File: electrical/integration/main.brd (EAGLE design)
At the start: 127 x 92 mm, 151 parts

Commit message: group components logically
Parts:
- moved POWER_TOP1:C2 558.5 mm to (-5.84, -14.9), flipped to the bottom, turned to 180 degrees
- moved POWER_TOP1:C3 529.0 mm to (5.52, -6.16), flipped to the bottom
- moved POWER_TOP1:R2 510.2 mm to (-9.82, -30.8), turned to 180 degrees
- moved POWER_TOP1:F2 493.8 mm to (-14.1, -14.9), flipped to the bottom
- moved POWER_TOP1:C4 480.6 mm to (36.3, -8.60), flipped to the bottom, turned to 270 degrees
- moved POWER_TOP1:R4 475.6 mm to (-12.4, 0.76), turned to 180 degrees
- moved POWER_TOP1:F1 469.6 mm to (28.1, -8.01), flipped to the bottom
- moved POWER_TOP1:MOV1 462.0 mm to (-5.66, -16.5), flipped to the bottom, turned to 180 degrees
- moved POWER_TOP1:LED1 455.6 mm to (-7.10, 0.70)
- moved POWER_TOP1:U$1 451.8 mm to (18.5, -3.90)
- moved POWER_TOP1:R3 445.0 mm to (36.4, -8.46), turned to 90 degrees
- moved POWER_TOP1:U$2 438.4 mm to (-9.63, -23.2), turned to 90 degrees
- moved POWER_TOP1:LED2 420.7 mm to (-4.43, -30.8)
- moved POWER_TOP1:MOV2 407.7 mm to (38.1, -8.58), flipped to the bottom, turned to 270 degrees
- moved MICROCONTROLLER1:R9 384.1 mm to (96.5, -67.3), turned to 90 degrees
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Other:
- board size 127 x 92 mm -> 168 x 104 mm

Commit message: replace mow enable toggle with connector. position connectors more
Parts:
- removed JETSON1:JETSON_TX2_J21_EXPANSION1:U$4, MICROCONTROLLER1:U$2, MICROCONTROLLER1:U$3: TSM-120-XX-XXX-DV, TSM-120-XX-XXX-DV:TSM-120-XX-XXX-D
- removed JETSON1:JETSON_TX2_J26_GPIO1:U$1, JETSON1:JETSON_TX2_J26_GPIO1:U$2: TSM-115-XX-XXX-DV, TSM-115-XX-XXX-DV:TSM-115-XX-XXX-D
- removed MOTOR_TOP1:MOTOR_ISO1:C3, MOTOR_TOP1:MOTOR_ISO2:C3: 1uF, rcl:C0603
- removed MOTOR_TOP1:MOTOR_ISO1:PAD1, MOTOR_TOP1:MOTOR_ISO2:PAD1: (no value), wirepad:1,6/0,8
- removed MOTOR_TOP1:MOTOR_ISO1:R1, MOTOR_TOP1:MOTOR_ISO1:R2, MOTOR_TOP1:MOTOR_ISO1:R5, MOTOR_TOP1:MOTOR_ISO2:R1, MOTOR_TOP1:MOTOR_ISO2:R2, MOTOR_TOP1:MOTOR_ISO2:R5: 47k, SparkFun-Resistors:0603
- removed MOTOR_TOP1:MOTOR_ISO1:R10, MOTOR_TOP1:MOTOR_ISO2:R10: 150k, SparkFun-Resistors:0603
- removed MOTOR_TOP1:MOTOR_ISO1:R3, MOTOR_TOP1:MOTOR_ISO1:R4, MOTOR_TOP1:MOTOR_ISO1:R6, MOTOR_TOP1:MOTOR_ISO1:R8, MOTOR_TOP1:MOTOR_ISO2:R3, MOTOR_TOP1:MOTOR_ISO2:R4, MOTOR_TOP1:MOTOR_ISO2:R6, MOTOR_TOP1:MOTOR_ISO2:R8: 1.20k, SparkFun-Resistors:0603
- removed MOTOR_TOP1:MOTOR_ISO1:R7, MOTOR_TOP1:MOTOR_ISO2:R7: 300k, SparkFun-Resistors:0603
- removed MOTOR_TOP1:MOTOR_ISO1:R9, MOTOR_TOP1:MOTOR_ISO2:R9: 330k, SparkFun-Resistors:0603
- removed MOTOR_TOP1:MOTOR_ISO1:U1, MOTOR_TOP1:MOTOR_ISO1:U2, MOTOR_TOP1:MOTOR_ISO1:U3, MOTOR_TOP1:MOTOR_ISO2:U1, MOTOR_TOP1:MOTOR_ISO2:U2, MOTOR_TOP1:MOTOR_ISO2:U3: SFH615A-3X009T, SFH615A-3X009T:SOIC254P1016X390-4N
- removed MOTOR_TOP1:MOTOR_ISO1:U4, MOTOR_TOP1:MOTOR_ISO2:U4: AMC1200SDUB, power_supplies:DUB8
- removed MOTOR_TOP1:MOTOR_ISO1:X1, MOTOR_TOP1:MOTOR_ISO2:X1: 43045-0609, con-molex-micro-fit-3_0:43045-0609
- removed RELAY_CONTROL_TOP1:RELAY_CONTROL1:S2: ST141D00, ST141D00:SW_ST141D00
- removed RELAY_CONTROL_TOP1:RELAY_CONTROL1:X1, RELAY_CONTROL_TOP1:RELAY_CONTROL1:X3, RELAY_CONTROL_TOP1:X3, RELAY_CONTROL_TOP1:X4: 43045-0209, con-molex-micro-fit-3_0:43045-0209
- added MOTOR_TOP1:JDL, MOTOR_TOP1:JDR: 43045-0609, con-molex-micro-fit-3_0:43045-0609
- added RELAY_CONTROL_TOP1:JBAT, RELAY_CONTROL_TOP1:JISO, RELAY_CONTROL_TOP1:RELAY_CONTROL1:JESTP, RELAY_CONTROL_TOP1:RELAY_CONTROL1:JMOW, RELAY_CONTROL_TOP1:RELAY_CONTROL1:JTHR: 43045-0209, con-molex-micro-fit-3_0:43045-0209
- moved SENSOR_TOP1:U1 97.9 mm to (91.6, -32.9)
- moved SENSOR_TOP1:ENCODER2:X1 97.6 mm to (24.0, -87.8)
- moved SENSOR_TOP1:ENCODER1:X1 97.5 mm to (40.9, -87.8)
- moved SENSOR_TOP1:REACH_GPS1:U$1 87.6 mm to (123.3, -77.9), turned to 90 degrees
- moved JETSON1:X1 84.7 mm to (-8.85, -45.5), turned to 0 degrees
- moved POWER_TOP1:R2 80.2 mm to (4.88, 48.0)
- moved POWER_TOP1:LED2 79.8 mm to (12.6, 47.2)
- moved RELAY_CONTROL_TOP1:RELAY_CONTROL1:D2 77.6 mm to (73.8, -6.02), flipped to the bottom, turned to 90 degrees
- moved RELAY_CONTROL_TOP1:RELAY_CONTROL1:R13 77.3 mm to (68.5, -10.7), flipped to the bottom, turned to 180 degrees
- moved RELAY_CONTROL_TOP1:RELAY_CONTROL1:D1 76.1 mm to (76.4, -6.24), flipped to the bottom, turned to 90 degrees
- moved RELAY_CONTROL_TOP1:RELAY_CONTROL1:R1 75.5 mm to (65.1, -10.7), flipped to the bottom, turned to 180 degrees
- moved RELAY_CONTROL_TOP1:RELAY_CONTROL1:RCCB2 75.2 mm to (70.0, -5.34), flipped to the bottom, turned to 90 degrees
- moved RELAY_CONTROL_TOP1:RELAY_CONTROL1:U$7 72.6 mm to (63.6, -5.06), flipped to the bottom, turned to 90 degrees
- moved RELAY_CONTROL_TOP1:RELAY_CONTROL1:RCCB1 71.6 mm to (79.8, -6.38), flipped to the bottom, turned to 90 degrees
- moved RELAY_CONTROL_TOP1:RELAY_CONTROL1:RCCM 71.2 mm to (57.4, -5.27), flipped to the bottom, turned to 270 degrees
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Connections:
- removed net JETSON1:JETSON_TX2_J26_GPIO1:AP2MDM_READY: JETSON1:JETSON_TX2_J26_GPIO1:U$1.6, JETSON1:JETSON_TX2_J26_GPIO1:U$2.6
- removed net JETSON1:JETSON_TX2_J26_GPIO1:CAN0_ERR: JETSON1:JETSON_TX2_J26_GPIO1:U$1.9, JETSON1:JETSON_TX2_J26_GPIO1:U$2.9
- removed net JETSON1:JETSON_TX2_J26_GPIO1:CAN0_RX: JETSON1:JETSON_TX2_J26_GPIO1:U$1.5, JETSON1:JETSON_TX2_J26_GPIO1:U$2.5
- removed net JETSON1:JETSON_TX2_J26_GPIO1:CAN0_STBY: JETSON1:JETSON_TX2_J26_GPIO1:U$1.3, JETSON1:JETSON_TX2_J26_GPIO1:U$2.3
- removed net JETSON1:JETSON_TX2_J26_GPIO1:CAN0_TX: JETSON1:JETSON_TX2_J26_GPIO1:U$1.7, JETSON1:JETSON_TX2_J26_GPIO1:U$2.7
- removed net JETSON1:JETSON_TX2_J26_GPIO1:CAN1_ERR: JETSON1:JETSON_TX2_J26_GPIO1:U$1.19, JETSON1:JETSON_TX2_J26_GPIO1:U$2.19
- removed net JETSON1:JETSON_TX2_J26_GPIO1:CAN1_RX: JETSON1:JETSON_TX2_J26_GPIO1:U$1.15, JETSON1:JETSON_TX2_J26_GPIO1:U$2.15
- removed net JETSON1:JETSON_TX2_J26_GPIO1:CAN1_STDBY: JETSON1:JETSON_TX2_J26_GPIO1:U$1.13, JETSON1:JETSON_TX2_J26_GPIO1:U$2.13
- removed net JETSON1:JETSON_TX2_J26_GPIO1:CAN1_TX: JETSON1:JETSON_TX2_J26_GPIO1:U$1.17, JETSON1:JETSON_TX2_J26_GPIO1:U$2.17
- removed net JETSON1:JETSON_TX2_J26_GPIO1:CAN_WAKE: JETSON1:JETSON_TX2_J26_GPIO1:U$1.1, JETSON1:JETSON_TX2_J26_GPIO1:U$2.1
- removed net JETSON1:JETSON_TX2_J26_GPIO1:DSPK_OUT_CLK: JETSON1:JETSON_TX2_J26_GPIO1:U$1.27, JETSON1:JETSON_TX2_J26_GPIO1:U$2.27
- removed net JETSON1:JETSON_TX2_J26_GPIO1:DSPK_OUT_DAT: JETSON1:JETSON_TX2_J26_GPIO1:U$1.29, JETSON1:JETSON_TX2_J26_GPIO1:U$2.29
- removed net JETSON1:JETSON_TX2_J26_GPIO1:GND: JETSON1:JETSON_TX2_J26_GPIO1:U$1.10, JETSON1:JETSON_TX2_J26_GPIO1:U$1.11, JETSON1:JETSON_TX2_J26_GPIO1:U$1.21, JETSON1:JETSON_TX2_J26_GPIO1:U$1.28, JETSON1:JETSON_TX2_J26_GPIO1:U$2.10, JETSON1:JETSON_TX2_J26_GPIO1:U$2.11, JETSON1:JETSON_TX2_J26_GPIO1:U$2.21, JETSON1:JETSON_TX2_J26_GPIO1:U$2.28
- removed net JETSON1:JETSON_TX2_J26_GPIO1:GNSS_PSS: JETSON1:JETSON_TX2_J26_GPIO1:U$1.30, JETSON1:JETSON_TX2_J26_GPIO1:U$2.30
- removed net JETSON1:JETSON_TX2_J26_GPIO1:I2C_GP2_CLK: JETSON1:JETSON_TX2_J26_GPIO1:U$1.12, JETSON1:JETSON_TX2_J26_GPIO1:U$2.12
- removed net JETSON1:JETSON_TX2_J26_GPIO1:I2C_GP2_DAT: JETSON1:JETSON_TX2_J26_GPIO1:U$1.14, JETSON1:JETSON_TX2_J26_GPIO1:U$2.14
- removed net JETSON1:JETSON_TX2_J26_GPIO1:I2C_GP3_CLK: JETSON1:JETSON_TX2_J26_GPIO1:U$1.18, JETSON1:JETSON_TX2_J26_GPIO1:U$2.18
- removed net JETSON1:JETSON_TX2_J26_GPIO1:I2C_GP3_DAT: JETSON1:JETSON_TX2_J26_GPIO1:U$1.20, JETSON1:JETSON_TX2_J26_GPIO1:U$2.20
- removed net JETSON1:JETSON_TX2_J26_GPIO1:I2S1_CLK: JETSON1:JETSON_TX2_J26_GPIO1:U$1.23, JETSON1:JETSON_TX2_J26_GPIO1:U$2.23
- removed net JETSON1:JETSON_TX2_J26_GPIO1:I2S1_LRCLK: JETSON1:JETSON_TX2_J26_GPIO1:U$1.26, JETSON1:JETSON_TX2_J26_GPIO1:U$2.26
- removed net JETSON1:JETSON_TX2_J26_GPIO1:I2S1_SDIN: JETSON1:JETSON_TX2_J26_GPIO1:U$1.25, JETSON1:JETSON_TX2_J26_GPIO1:U$2.25
- removed net JETSON1:JETSON_TX2_J26_GPIO1:I2S1_SDOUT: JETSON1:JETSON_TX2_J26_GPIO1:U$1.24, JETSON1:JETSON_TX2_J26_GPIO1:U$2.24
- removed net JETSON1:JETSON_TX2_J26_GPIO1:SLEEP: JETSON1:JETSON_TX2_J26_GPIO1:U$1.22, JETSON1:JETSON_TX2_J26_GPIO1:U$2.22
- removed net JETSON1:JETSON_TX2_J26_GPIO1:VDD_1V8: JETSON1:JETSON_TX2_J26_GPIO1:U$1.4, JETSON1:JETSON_TX2_J26_GPIO1:U$2.4
- removed net JETSON1:JETSON_TX2_J26_GPIO1:VDD_3V3_SYS: JETSON1:JETSON_TX2_J26_GPIO1:U$1.2, JETSON1:JETSON_TX2_J26_GPIO1:U$2.2
- removed net JETSON1:JETSON_TX2_J26_GPIO1:VDD_5V0_IO_SYS: JETSON1:JETSON_TX2_J26_GPIO1:U$1.8, JETSON1:JETSON_TX2_J26_GPIO1:U$2.8
- removed net JETSON1:JETSON_TX2_J26_GPIO1:WDT_TIME_OUT_L: JETSON1:JETSON_TX2_J26_GPIO1:U$1.16, JETSON1:JETSON_TX2_J26_GPIO1:U$2.16
- removed net MICROCONTROLLER1:RX2: MICROCONTROLLER1:U$2.35
- removed net MOTOR_TOP1:MOTOR_ISO1:CURRENT_SENSE: MOTOR_TOP1:MOTOR_ISO1:C3.1, MOTOR_TOP1:MOTOR_ISO1:R8.1
- removed net MOTOR_TOP1:MOTOR_ISO1:ENABLE: MOTOR_TOP1:MOTOR_ISO1:R6.1
- removed net MOTOR_TOP1:MOTOR_ISO1:MOTOR_ISENSE: MOTOR_TOP1:MOTOR_ISO1:R10.2, MOTOR_TOP1:MOTOR_ISO1:X1.P$5
- removed net MOTOR_TOP1:MOTOR_ISO1:MOW_EN_ISO: MOTOR_TOP1:MOTOR_ISO1:R1.2, MOTOR_TOP1:MOTOR_ISO1:U2.3, MOTOR_TOP1:MOTOR_ISO1:X1.P$2
- removed net MOTOR_TOP1:MOTOR_ISO1:MOW_EN_ISO1: MOTOR_TOP1:MOTOR_ISO1:R2.2, MOTOR_TOP1:MOTOR_ISO1:U1.3, MOTOR_TOP1:MOTOR_ISO1:X1.P$3
- removed net MOTOR_TOP1:MOTOR_ISO1:MOW_EN_ISO2: MOTOR_TOP1:MOTOR_ISO1:R5.2, MOTOR_TOP1:MOTOR_ISO1:U3.3, MOTOR_TOP1:MOTOR_ISO1:X1.P$4
- removed net MOTOR_TOP1:MOTOR_ISO1:N$1: MOTOR_TOP1:MOTOR_ISO1:R3.2, MOTOR_TOP1:MOTOR_ISO1:U2.1
- removed net MOTOR_TOP1:MOTOR_ISO1:N$2: MOTOR_TOP1:MOTOR_ISO1:R4.2, MOTOR_TOP1:MOTOR_ISO1:U1.1
- removed net MOTOR_TOP1:MOTOR_ISO1:N$3: MOTOR_TOP1:MOTOR_ISO1:R6.2, MOTOR_TOP1:MOTOR_ISO1:U3.1
- removed net MOTOR_TOP1:MOTOR_ISO1:N$4: MOTOR_TOP1:MOTOR_ISO1:R8.2, MOTOR_TOP1:MOTOR_ISO1:U4.7
- removed net MOTOR_TOP1:MOTOR_ISO1:N$5: MOTOR_TOP1:MOTOR_ISO1:R9.2, MOTOR_TOP1:MOTOR_ISO1:U4.6
- removed net MOTOR_TOP1:MOTOR_ISO1:N$6: MOTOR_TOP1:MOTOR_ISO1:R10.1, MOTOR_TOP1:MOTOR_ISO1:R7.2, MOTOR_TOP1:MOTOR_ISO1:U4.2
- removed net MOTOR_TOP1:MOTOR_ISO1:N$7: MOTOR_TOP1:MOTOR_ISO1:PAD1.1, MOTOR_TOP1:MOTOR_ISO1:U4.1
- removed net MOTOR_TOP1:MOTOR_ISO1:PWM_A: MOTOR_TOP1:MOTOR_ISO1:R3.1
- removed net MOTOR_TOP1:MOTOR_ISO1:PWM_B: MOTOR_TOP1:MOTOR_ISO1:R4.1
- removed net MOTOR_TOP1:MOTOR_ISO2:CURRENT_SENSE: MOTOR_TOP1:MOTOR_ISO2:C3.1, MOTOR_TOP1:MOTOR_ISO2:R8.1
- removed net MOTOR_TOP1:MOTOR_ISO2:ENABLE: MOTOR_TOP1:MOTOR_ISO2:R6.1
- removed net MOTOR_TOP1:MOTOR_ISO2:MOTOR_ISENSE: MOTOR_TOP1:MOTOR_ISO2:R10.2, MOTOR_TOP1:MOTOR_ISO2:X1.P$5
- removed net MOTOR_TOP1:MOTOR_ISO2:MOW_EN_ISO: MOTOR_TOP1:MOTOR_ISO2:R1.2, MOTOR_TOP1:MOTOR_ISO2:U2.3, MOTOR_TOP1:MOTOR_ISO2:X1.P$2
- removed net MOTOR_TOP1:MOTOR_ISO2:MOW_EN_ISO1: MOTOR_TOP1:MOTOR_ISO2:R2.2, MOTOR_TOP1:MOTOR_ISO2:U1.3, MOTOR_TOP1:MOTOR_ISO2:X1.P$3
- removed net MOTOR_TOP1:MOTOR_ISO2:MOW_EN_ISO2: MOTOR_TOP1:MOTOR_ISO2:R5.2, MOTOR_TOP1:MOTOR_ISO2:U3.3, MOTOR_TOP1:MOTOR_ISO2:X1.P$4
- removed net MOTOR_TOP1:MOTOR_ISO2:N$1: MOTOR_TOP1:MOTOR_ISO2:R3.2, MOTOR_TOP1:MOTOR_ISO2:U2.1
- removed net MOTOR_TOP1:MOTOR_ISO2:N$2: MOTOR_TOP1:MOTOR_ISO2:R4.2, MOTOR_TOP1:MOTOR_ISO2:U1.1
- removed net MOTOR_TOP1:MOTOR_ISO2:N$3: MOTOR_TOP1:MOTOR_ISO2:R6.2, MOTOR_TOP1:MOTOR_ISO2:U3.1
- removed net MOTOR_TOP1:MOTOR_ISO2:N$4: MOTOR_TOP1:MOTOR_ISO2:R8.2, MOTOR_TOP1:MOTOR_ISO2:U4.7
- removed net MOTOR_TOP1:MOTOR_ISO2:N$5: MOTOR_TOP1:MOTOR_ISO2:R9.2, MOTOR_TOP1:MOTOR_ISO2:U4.6
- removed net MOTOR_TOP1:MOTOR_ISO2:N$6: MOTOR_TOP1:MOTOR_ISO2:R10.1, MOTOR_TOP1:MOTOR_ISO2:R7.2, MOTOR_TOP1:MOTOR_ISO2:U4.2
- removed net MOTOR_TOP1:MOTOR_ISO2:N$7: MOTOR_TOP1:MOTOR_ISO2:PAD1.1, MOTOR_TOP1:MOTOR_ISO2:U4.1
- removed net MOTOR_TOP1:MOTOR_ISO2:PWM_A: MOTOR_TOP1:MOTOR_ISO2:R3.1
- removed net MOTOR_TOP1:MOTOR_ISO2:PWM_B: MOTOR_TOP1:MOTOR_ISO2:R4.1
- net 5V: now also MOTOR_TOP1:JDL.P$1, MOTOR_TOP1:JDR.P$1; no longer MOTOR_TOP1:MOTOR_ISO1:U4.8, MOTOR_TOP1:MOTOR_ISO2:U4.8
- net 5V_ISO: no longer MOTOR_TOP1:MOTOR_ISO1:U1.4, MOTOR_TOP1:MOTOR_ISO1:U2.4, MOTOR_TOP1:MOTOR_ISO1:U3.4, MOTOR_TOP1:MOTOR_ISO2:U1.4, MOTOR_TOP1:MOTOR_ISO2:U2.4, MOTOR_TOP1:MOTOR_ISO2:U3.4
- net GND: now also MOTOR_TOP1:JDL.P$6, MOTOR_TOP1:JDR.P$6, RELAY_CONTROL_TOP1:JBAT.P$1; no longer JETSON1:JETSON_TX2_J21_EXPANSION1:U$4.14, JETSON1:JETSON_TX2_J21_EXPANSION1:U$4.20, JETSON1:JETSON_TX2_J21_EXPANSION1:U$4.25, JETSON1:JETSON_TX2_J21_EXPANSION1:U$4.30, JETSON1:JETSON_TX2_J21_EXPANSION1:U$4.34, JETSON1:JETSON_TX2_J21_EXPANSION1:U$4.39, JETSON1:JETSON_TX2_J21_EXPANSION1:U$4.6, JETSON1:JETSON_TX2_J21_EXPANSION1:U$4.9, MOTOR_TOP1:MOTOR_ISO1:C3.2, MOTOR_TOP1:MOTOR_ISO1:R9.1, MOTOR_TOP1:MOTOR_ISO1:U1.2, MOTOR_TOP1:MOTOR_ISO1:U2.2, MOTOR_TOP1:MOTOR_ISO1:U3.2, MOTOR_TOP1:MOTOR_ISO1:U4.5, MOTOR_TOP1:MOTOR_ISO2:C3.2, MOTOR_TOP1:MOTOR_ISO2:R9.1, MOTOR_TOP1:MOTOR_ISO2:U1.2, MOTOR_TOP1:MOTOR_ISO2:U2.2, MOTOR_TOP1:MOTOR_ISO2:U3.2, MOTOR_TOP1:MOTOR_ISO2:U4.5, RELAY_CONTROL_TOP1:X3.P$1
- net GND_ISO: now also RELAY_CONTROL_TOP1:JISO.P$1; no longer MOTOR_TOP1:MOTOR_ISO1:R1.1, MOTOR_TOP1:MOTOR_ISO1:R2.1, MOTOR_TOP1:MOTOR_ISO1:R5.1, MOTOR_TOP1:MOTOR_ISO1:R7.1, MOTOR_TOP1:MOTOR_ISO1:U4.3, MOTOR_TOP1:MOTOR_ISO1:U4.4, MOTOR_TOP1:MOTOR_ISO1:X1.P$6, MOTOR_TOP1:MOTOR_ISO2:R1.1, MOTOR_TOP1:MOTOR_ISO2:R2.1, MOTOR_TOP1:MOTOR_ISO2:R5.1, MOTOR_TOP1:MOTOR_ISO2:R7.1, MOTOR_TOP1:MOTOR_ISO2:U4.3, MOTOR_TOP1:MOTOR_ISO2:U4.4, MOTOR_TOP1:MOTOR_ISO2:X1.P$6, RELAY_CONTROL_TOP1:X4.P$1
- net JETSON1:JETSON_TX2_J21_EXPANSION1:AO_DMIC_IN_CLK_LVL: no longer JETSON1:JETSON_TX2_J21_EXPANSION1:U$4.32
- net JETSON1:JETSON_TX2_J21_EXPANSION1:AO_DMIC_IN_DAT_LVL: no longer JETSON1:JETSON_TX2_J21_EXPANSION1:U$4.16
- net JETSON1:JETSON_TX2_J21_EXPANSION1:AP_WAKE_BT_3V3: no longer JETSON1:JETSON_TX2_J21_EXPANSION1:U$4.33
- net JETSON1:JETSON_TX2_J21_EXPANSION1:AUDIO_CDC_IRQ_LVL: no longer JETSON1:JETSON_TX2_J21_EXPANSION1:U$4.13
- net JETSON1:JETSON_TX2_J21_EXPANSION1:AUDIO_I2S_MCLK_3V3: no longer JETSON1:JETSON_TX2_J21_EXPANSION1:U$4.7
- net JETSON1:JETSON_TX2_J21_EXPANSION1:AUDIO_I2S_SFSYNC_3V3: no longer JETSON1:JETSON_TX2_J21_EXPANSION1:U$4.35
- net JETSON1:JETSON_TX2_J21_EXPANSION1:AUDIO_I2S_SIN_3V3: no longer JETSON1:JETSON_TX2_J21_EXPANSION1:U$4.38
- net JETSON1:JETSON_TX2_J21_EXPANSION1:AUDIO_I2S_SOUT_3V3: no longer JETSON1:JETSON_TX2_J21_EXPANSION1:U$4.40
- net JETSON1:JETSON_TX2_J21_EXPANSION1:AUDIO_I2S_SRCLK_3V3: no longer JETSON1:JETSON_TX2_J21_EXPANSION1:U$4.12
- net JETSON1:JETSON_TX2_J21_EXPANSION1:AUD_RST_LVL: no longer JETSON1:JETSON_TX2_J21_EXPANSION1:U$4.29
- net JETSON1:JETSON_TX2_J21_EXPANSION1:GPIO_EXP_P16_3V3: no longer JETSON1:JETSON_TX2_J21_EXPANSION1:U$4.22
- net JETSON1:JETSON_TX2_J21_EXPANSION1:GPIO_EXP_P17_3V3: no longer JETSON1:JETSON_TX2_J21_EXPANSION1:U$4.15
- net JETSON1:JETSON_TX2_J21_EXPANSION1:I2C_GP1_CLK_3V3: no longer JETSON1:JETSON_TX2_J21_EXPANSION1:U$4.28
- net JETSON1:JETSON_TX2_J21_EXPANSION1:I2C_GP1_DAT_3V3: no longer JETSON1:JETSON_TX2_J21_EXPANSION1:U$4.27
- net JETSON1:JETSON_TX2_J21_EXPANSION1:MDM_WAKE_AP_LVL: no longer JETSON1:JETSON_TX2_J21_EXPANSION1:U$4.18
- net JETSON1:JETSON_TX2_J21_EXPANSION1:MOTION_INT_AP_L_LVL: no longer JETSON1:JETSON_TX2_J21_EXPANSION1:U$4.31
- net JETSON1:JETSON_TX2_J21_EXPANSION1:SAR_TOUT_LVL: no longer JETSON1:JETSON_TX2_J21_EXPANSION1:U$4.37
- net JETSON1:JETSON_TX2_J21_EXPANSION1:SPI1_CS0_3V3: no longer JETSON1:JETSON_TX2_J21_EXPANSION1:U$4.24
- net JETSON1:JETSON_TX2_J21_EXPANSION1:SPI1_MISO_3V3: no longer JETSON1:JETSON_TX2_J21_EXPANSION1:U$4.21
- net JETSON1:JETSON_TX2_J21_EXPANSION1:SPI1_MOSI_3V3: no longer JETSON1:JETSON_TX2_J21_EXPANSION1:U$4.19
- net JETSON1:JETSON_TX2_J21_EXPANSION1:SPI1_SCK_3V3: no longer JETSON1:JETSON_TX2_J21_EXPANSION1:U$4.23
- net JETSON1:JETSON_TX2_J21_EXPANSION1:UART1_CTS_HDR_3V3: no longer JETSON1:JETSON_TX2_J21_EXPANSION1:U$4.36
- net JETSON1:JETSON_TX2_J21_EXPANSION1:UART1_RTS_HDR_3V3: no longer JETSON1:JETSON_TX2_J21_EXPANSION1:U$4.11
- net JETSON1:JETSON_TX2_J21_EXPANSION1:VDD_3V3_SYS: no longer JETSON1:JETSON_TX2_J21_EXPANSION1:U$4.1, JETSON1:JETSON_TX2_J21_EXPANSION1:U$4.17
- net JETSON1:JETSON_TX2_J21_EXPANSION1:VDD_5V0_IO_SYS: no longer JETSON1:JETSON_TX2_J21_EXPANSION1:U$4.2, JETSON1:JETSON_TX2_J21_EXPANSION1:U$4.4
- net MICROCONTROLLER1:10: no longer MICROCONTROLLER1:U$2.21
- net MICROCONTROLLER1:11: no longer MICROCONTROLLER1:U$2.23
- net MICROCONTROLLER1:12: no longer MICROCONTROLLER1:U$2.25
- net MICROCONTROLLER1:13: no longer MICROCONTROLLER1:U$2.27
- net MICROCONTROLLER1:35: no longer MICROCONTROLLER1:U$2.32
- net MICROCONTROLLER1:36: no longer MICROCONTROLLER1:U$2.34
- net MICROCONTROLLER1:37: no longer MICROCONTROLLER1:U$2.36
- net MICROCONTROLLER1:38: no longer MICROCONTROLLER1:U$2.38
- net MICROCONTROLLER1:39: no longer MICROCONTROLLER1:U$2.40
- net MICROCONTROLLER1:40: no longer MICROCONTROLLER1:U$3.1
- net MICROCONTROLLER1:41: no longer MICROCONTROLLER1:U$3.3
- net MICROCONTROLLER1:42: no longer MICROCONTROLLER1:U$3.5
- net MICROCONTROLLER1:43: no longer MICROCONTROLLER1:U$3.7
- net MICROCONTROLLER1:44: no longer MICROCONTROLLER1:U$3.9
- net MICROCONTROLLER1:45: no longer MICROCONTROLLER1:U$3.11
- net MICROCONTROLLER1:46: no longer MICROCONTROLLER1:U$3.13
- net MICROCONTROLLER1:47: no longer MICROCONTROLLER1:U$3.15
- net MICROCONTROLLER1:48: no longer MICROCONTROLLER1:U$3.17
- net MICROCONTROLLER1:49: no longer MICROCONTROLLER1:U$3.19
- net MICROCONTROLLER1:50: no longer MICROCONTROLLER1:U$3.21
- net MICROCONTROLLER1:51: no longer MICROCONTROLLER1:U$3.23
- net MICROCONTROLLER1:52: no longer MICROCONTROLLER1:U$3.25
- net MICROCONTROLLER1:53: no longer MICROCONTROLLER1:U$3.27
- net MICROCONTROLLER1:9: no longer MICROCONTROLLER1:U$2.19
- net MICROCONTROLLER1:A10: no longer MICROCONTROLLER1:U$3.10
- net MICROCONTROLLER1:A11: no longer MICROCONTROLLER1:U$3.12
- net MICROCONTROLLER1:A9: no longer MICROCONTROLLER1:U$3.8
- net MICROCONTROLLER1:CANRX: no longer MICROCONTROLLER1:U$3.18
- net MICROCONTROLLER1:CANTX: no longer MICROCONTROLLER1:U$3.20
- net MICROCONTROLLER1:DAC0: no longer MICROCONTROLLER1:U$3.14
- net MICROCONTROLLER1:DAC1: no longer MICROCONTROLLER1:U$3.16
- net MICROCONTROLLER1:LED_SCL: no longer MICROCONTROLLER1:U$2.4
- net MICROCONTROLLER1:LED_SDA: no longer MICROCONTROLLER1:U$2.2
- net MICROCONTROLLER1:MISO: no longer MICROCONTROLLER1:U$3.26
- net MICROCONTROLLER1:MOSI: no longer MICROCONTROLLER1:U$3.28
- net MICROCONTROLLER1:RX3: no longer MICROCONTROLLER1:U$2.31
- net MICROCONTROLLER1:SCK: no longer MICROCONTROLLER1:U$3.30
- net MICROCONTROLLER1:SCL1: no longer MICROCONTROLLER1:U$3.24
- net MICROCONTROLLER1:SDA1: no longer MICROCONTROLLER1:U$3.22
- net MICROCONTROLLER1:TX0: no longer MICROCONTROLLER1:U$2.3
- net MICROCONTROLLER1:TX2: no longer MICROCONTROLLER1:U$2.33
- net MICROCONTROLLER1:TX3: no longer MICROCONTROLLER1:U$2.29
- net MOW_EN: no longer MICROCONTROLLER1:U$2.18
- net N$1: now also MOTOR_TOP1:JDR.P$3; no longer MICROCONTROLLER1:U$2.11
- net N$10: no longer MICROCONTROLLER1:U$2.30
- net N$11: no longer MICROCONTROLLER1:U$2.17
- net N$12: no longer MICROCONTROLLER1:U$3.6
- net N$13: no longer MICROCONTROLLER1:U$3.4
- net N$14: no longer MICROCONTROLLER1:U$3.2
- net N$15: no longer MICROCONTROLLER1:U$3.39
- net N$16: no longer MICROCONTROLLER1:U$2.15
- net N$17: no longer MICROCONTROLLER1:U$2.26
- net N$18: no longer MICROCONTROLLER1:U$2.24
- net N$19: no longer JETSON1:JETSON_TX2_J21_EXPANSION1:U$4.5
- net N$2: no longer JETSON1:JETSON_TX2_J21_EXPANSION1:U$4.10
- net N$20: no longer JETSON1:JETSON_TX2_J21_EXPANSION1:U$4.3
- net N$21: no longer MICROCONTROLLER1:U$3.37
- net N$22: no longer MICROCONTROLLER1:U$3.35
- net N$23: no longer MICROCONTROLLER1:U$2.13
- net N$24: no longer MICROCONTROLLER1:U$2.22
- net N$25: no longer MICROCONTROLLER1:U$2.20
- net N$26: now also MOTOR_TOP1:JDL.P$3; no longer MICROCONTROLLER1:U$2.7
- net N$27: now also MOTOR_TOP1:JDL.P$2; no longer MICROCONTROLLER1:U$2.5
- net N$28: no longer MICROCONTROLLER1:U$2.39
- net N$29: no longer MICROCONTROLLER1:U$2.37
- net N$3: now also MOTOR_TOP1:JDL.P$4; no longer MICROCONTROLLER1:U$2.6
- net N$30: no longer MICROCONTROLLER1:U$2.1
- net N$31: no longer MICROCONTROLLER1:U$2.8
- net N$32: no longer MICROCONTROLLER1:U$2.10
- net N$33: no longer MICROCONTROLLER1:U$2.14
- net N$34: no longer MICROCONTROLLER1:U$2.16
- net N$4: now also MOTOR_TOP1:JDL.P$5; no longer MICROCONTROLLER1:U$3.29
- net N$5: now also MOTOR_TOP1:JDR.P$2; no longer MICROCONTROLLER1:U$2.9
- net N$6: no longer JETSON1:JETSON_TX2_J21_EXPANSION1:U$4.8
- net N$7: now also MOTOR_TOP1:JDR.P$4; no longer MICROCONTROLLER1:U$2.12
- net N$8: now also MOTOR_TOP1:JDR.P$5; no longer MICROCONTROLLER1:U$3.31
- net N$9: no longer MICROCONTROLLER1:U$2.28
- net RELAY_CONTROL_TOP1:36V_RAW: now also RELAY_CONTROL_TOP1:JISO.P$2, RELAY_CONTROL_TOP1:RELAY_CONTROL1:JTHR.P$2; no longer RELAY_CONTROL_TOP1:RELAY_CONTROL1:X1.P$2, RELAY_CONTROL_TOP1:X4.P$2
- net RELAY_CONTROL_TOP1:N$1: now also RELAY_CONTROL_TOP1:JBAT.P$2; no longer RELAY_CONTROL_TOP1:X3.P$2
- net RELAY_CONTROL_TOP1:N$2: now also RELAY_CONTROL_TOP1:RELAY_CONTROL1:JMOW.P$1; no longer RELAY_CONTROL_TOP1:RELAY_CONTROL1:S2.1
- net RELAY_CONTROL_TOP1:N$3: now also RELAY_CONTROL_TOP1:RELAY_CONTROL1:JESTP.P$1, RELAY_CONTROL_TOP1:RELAY_CONTROL1:JMOW.P$2; no longer RELAY_CONTROL_TOP1:RELAY_CONTROL1:S2.3, RELAY_CONTROL_TOP1:RELAY_CONTROL1:X3.P$1
- net RELAY_CONTROL_TOP1:RELAY_CONTROL1:N$1: now also RELAY_CONTROL_TOP1:RELAY_CONTROL1:JESTP.P$2, RELAY_CONTROL_TOP1:RELAY_CONTROL1:JTHR.P$1; no longer RELAY_CONTROL_TOP1:RELAY_CONTROL1:X1.P$1, RELAY_CONTROL_TOP1:RELAY_CONTROL1:X3.P$2
- net VSENSE: no longer MICROCONTROLLER1:U$3.33

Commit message: make output connector names more clearer
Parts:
- renumbered RELAY_CONTROL_TOP1:X1 to RELAY_CONTROL_TOP1:JDC, RELAY_CONTROL_TOP1:X2 to RELAY_CONTROL_TOP1:JMC
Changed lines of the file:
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@@
 <element name="RELAY_CONTROL_TOP1:RELAY_CONTROL1:JTHR" library="con-molex-micro-fit-3_0" package="43045-0209" value="43045-0209" x="93.83" y="-5.04" rot="R180"/>
 <element name="RELAY_CONTROL_TOP1:RELAY_CONTROL1:JESTP" library="con-molex-micro-fit-3_0" package="43045-0209" value="43045-0209" x="81.86" y="-5.04" rot="R180"/>
-<element name="RELAY_CONTROL_TOP1:X1" library="con-molex-micro-fit-3_0" package="43045-0209" value="43045-0209" x="42.69" y="-4.82" rot="R180"/>
-<element name="RELAY_CONTROL_TOP1:X2" library="con-molex-micro-fit-3_0" package="43045-0209" value="43045-0209" x="57.32" y="-4.82" rot="R180"/>
+<element name="RELAY_CONTROL_TOP1:JDC" library="con-molex-micro-fit-3_0" package="43045-0209" value="43045-0209" x="42.69" y="-4.82" rot="R180"/>
+<element name="RELAY_CONTROL_TOP1:JMC" library="con-molex-micro-fit-3_0" package="43045-0209" value="43045-0209" x="57.32" y="-4.82" rot="R180"/>
 <element name="RELAY_CONTROL_TOP1:JBAT" library="con-molex-micro-fit-3_0" package="43045-0209" value="43045-0209" x="29.55" y="-4.37" rot="R180"/>
 <element name="RELAY_CONTROL_TOP1:JISO" library="con-molex-micro-fit-3_0" package="43045-0209" value="43045-0209" x="29.42" y="-4.32" rot="MR180"/>
@@
 <signal name="RELAY_CONTROL_TOP1:N$2">
 <contactref element="RELAY_CONTROL_TOP1:RELAY_CONTROL1:D2" pad="C"/>
-<contactref element="RELAY_CONTROL_TOP1:X2" pad="P$1"/>
+<contactref element="RELAY_CONTROL_TOP1:JMC" pad="P$1"/>
 <contactref element="RELAY_CONTROL_TOP1:RELAY_CONTROL1:JMOW" pad="P$1"/>
 <wire x1="57.32" y1="-10.29" x2="69.6" y2="-10.27" width="0" layer="19" extent="1-1"/>
@@
 <contactref element="RELAY_CONTROL_TOP1:RELAY_CONTROL1:RCCB2" pad="2"/>
 <contactref element="RELAY_CONTROL_TOP1:RELAY_CONTROL1:D2" pad="A"/>
-<contactref element="RELAY_CONTROL_TOP1:X2" pad="P$2"/>
+<contactref element="RELAY_CONTROL_TOP1:JMC" pad="P$2"/>
 <wire x1="73.8" y1="-4.77" x2="57.32" y2="-14.92" width="0" layer="19" extent="1-1"/>
 <wire x1="69.95" y1="-2.54" x2="73.8" y2="-4.77" width="0" layer="19" extent="1-1"/>
@@
 <contactref element="RELAY_CONTROL_TOP1:RELAY_CONTROL1:JESTP" pad="P$1"/>
 <contactref element="RELAY_CONTROL_TOP1:RELAY_CONTROL1:D1" pad="C"/>
-<contactref element="RELAY_CONTROL_TOP1:X1" pad="P$1"/>
+<contactref element="RELAY_CONTROL_TOP1:JDC" pad="P$1"/>
 <contactref element="RELAY_CONTROL_TOP1:RELAY_CONTROL1:JMOW" pad="P$2"/>
 <wire x1="42.69" y1="-10.29" x2="69.6" y2="-14.9" width="0" layer="19" extent="1-1"/>
@@
 <contactref element="RELAY_CONTROL_TOP1:RELAY_CONTROL1:RCCB1" pad="2"/>
 <contactref element="RELAY_CONTROL_TOP1:RELAY_CONTROL1:D1" pad="A"/>
-<contactref element="RELAY_CONTROL_TOP1:X1" pad="P$2"/>
+<contactref element="RELAY_CONTROL_TOP1:JDC" pad="P$2"/>
 <wire x1="79.85" y1="-3.58" x2="76.4" y2="-4.99" width="0" layer="19" extent="1-1"/>
 <wire x1="42.69" y1="-14.92" x2="79.85" y2="-3.58" width="0" layer="19" extent="1-1"/>

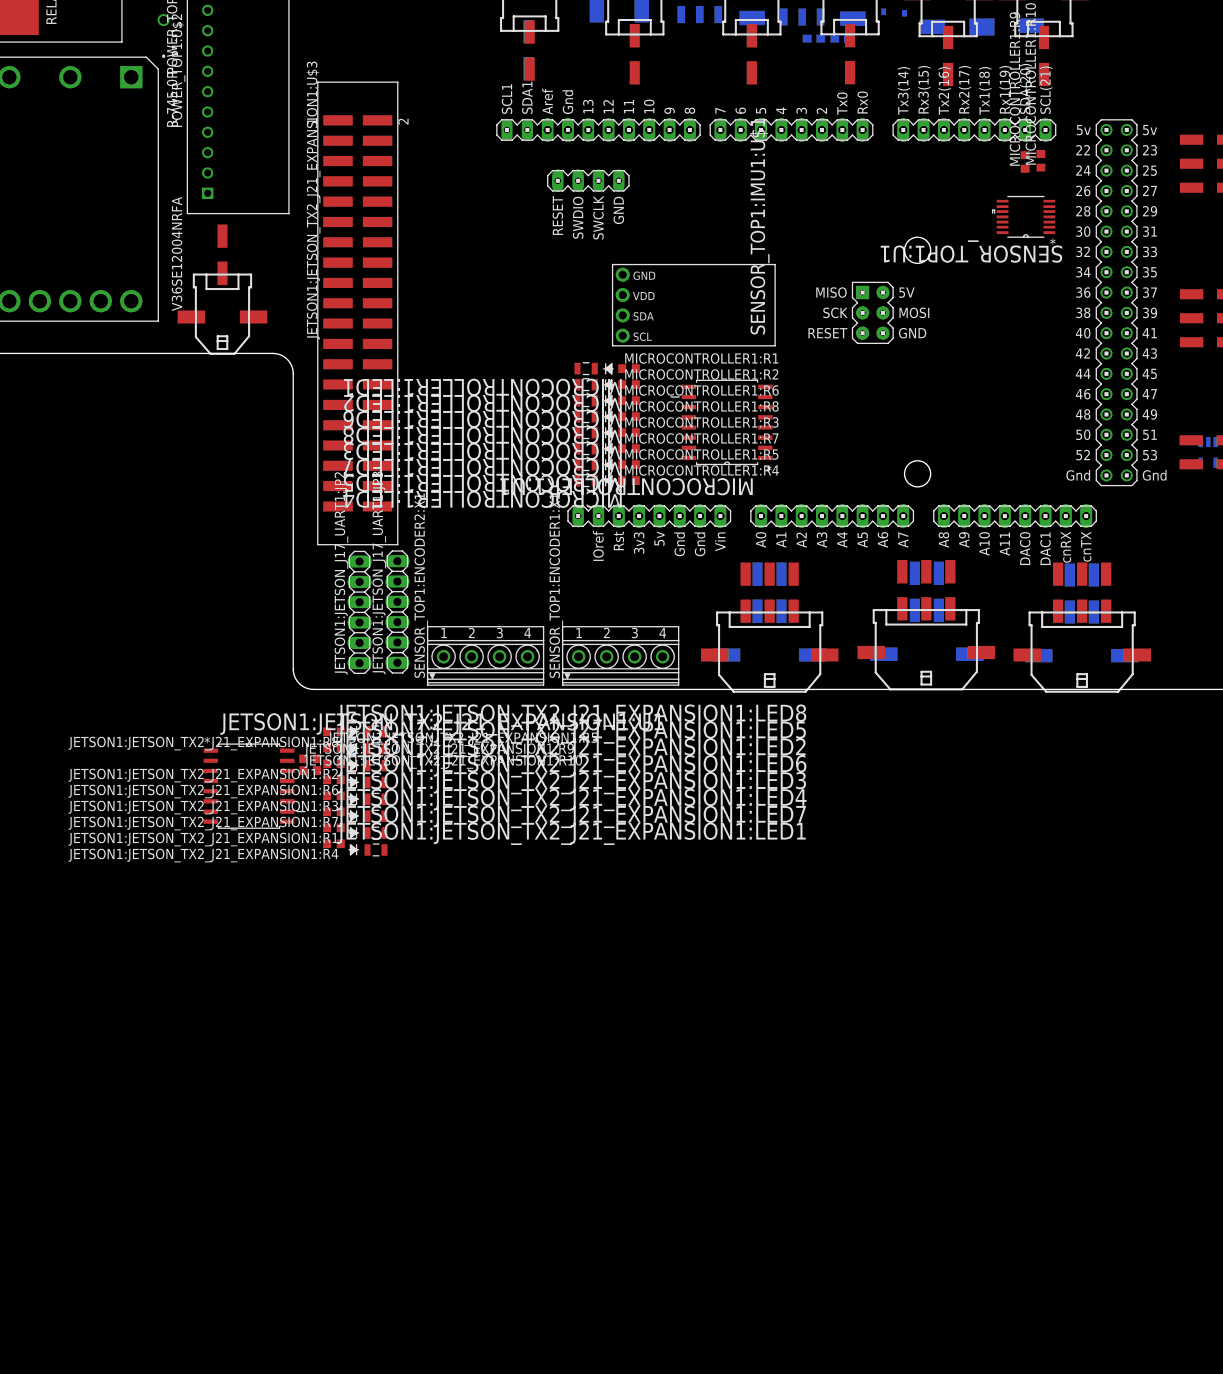
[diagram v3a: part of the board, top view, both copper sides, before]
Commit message: bamboozled, arduino due become mega
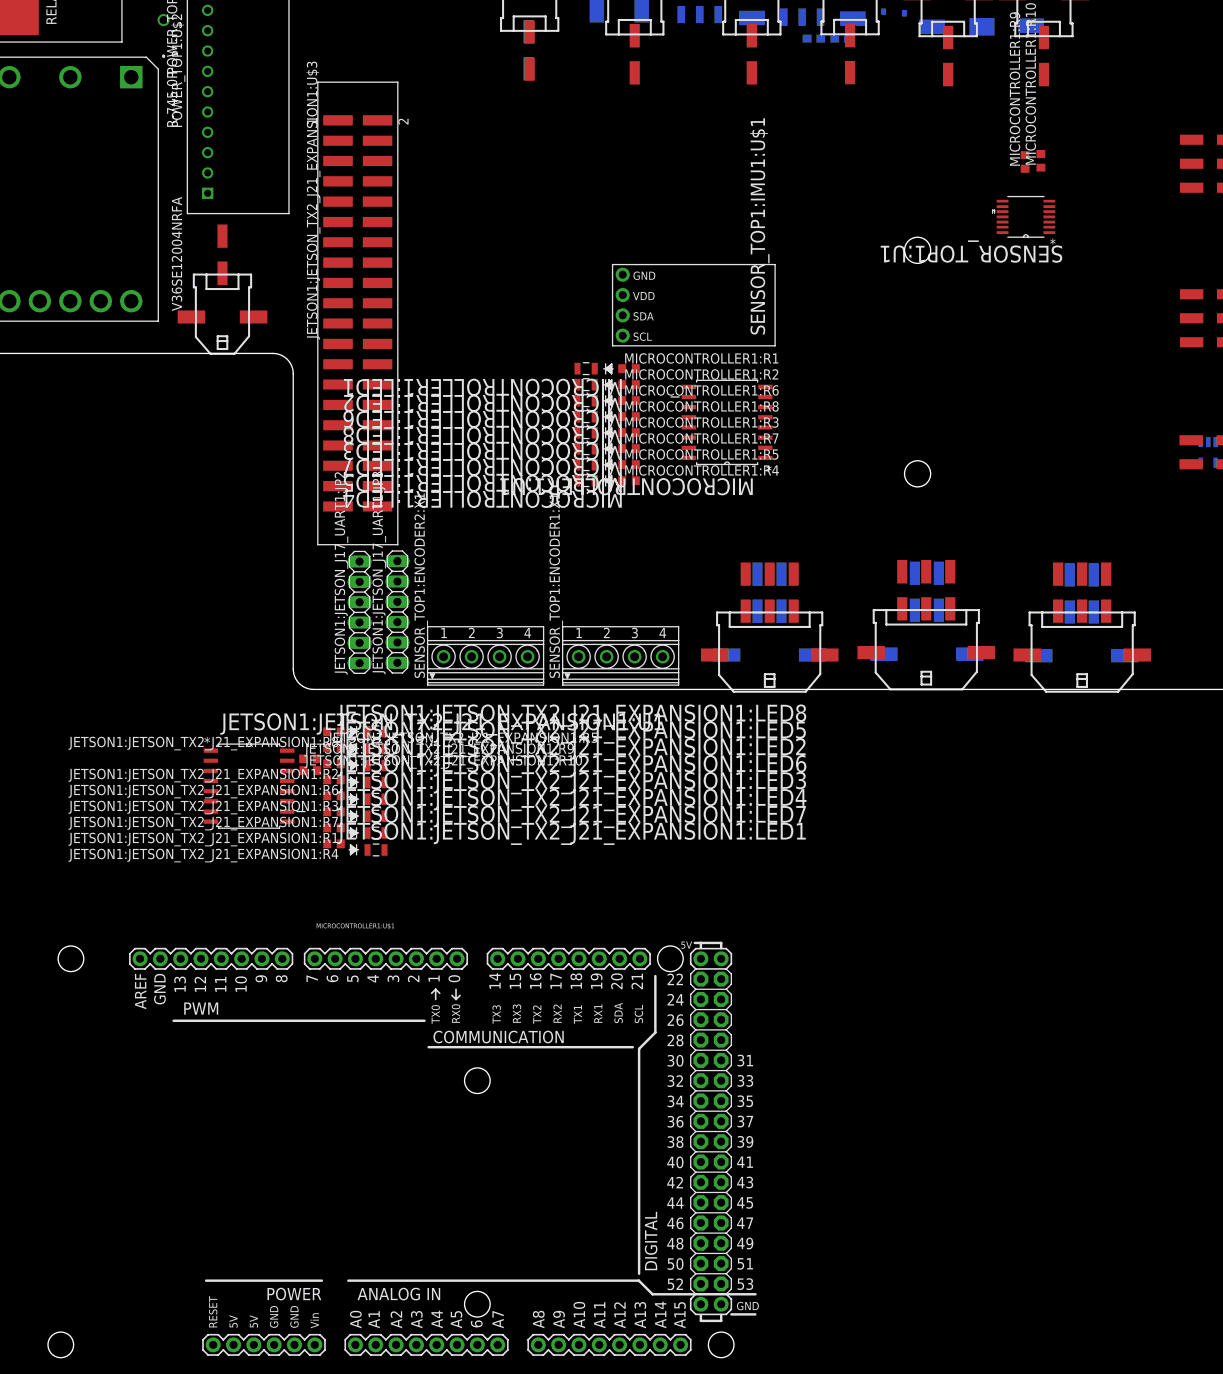
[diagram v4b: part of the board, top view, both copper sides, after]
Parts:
- MICROCONTROLLER1:U$1: value DUE(NORMAL) -> ARDUINO_MEGA_R3FULL; device DUElib130425:DUE(NORMAL) -> SparkFun-Boards:ARDUINO_MEGA
- moved MICROCONTROLLER1:U$1 123.5 mm to (6.50, -149.8)
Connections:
- net MICROCONTROLLER1:N$25 renamed MICROCONTROLLER1:N$2
- removed net MICROCONTROLLER1:5VA: MICROCONTROLLER1:U$1.5V_A
- removed net MICROCONTROLLER1:5VB: MICROCONTROLLER1:U$1.5V_B
- removed net MICROCONTROLLER1:CANRX: MICROCONTROLLER1:U$1.CANRX
- removed net MICROCONTROLLER1:CANTX: MICROCONTROLLER1:U$1.CANTX
- removed net MICROCONTROLLER1:DAC0: MICROCONTROLLER1:U$1.DAC0
- removed net MICROCONTROLLER1:DAC1: MICROCONTROLLER1:U$1.DAC1
- removed net MICROCONTROLLER1:DBGGND: MICROCONTROLLER1:U$1.GND_DEBUG
- removed net MICROCONTROLLER1:DBGRST: MICROCONTROLLER1:U$1.RESET_DEBUG
- removed net MICROCONTROLLER1:DBGSDIO: MICROCONTROLLER1:U$1.SWDIO_DEBUG
- removed net MICROCONTROLLER1:DBGSWCLK: MICROCONTROLLER1:U$1.SWCLK_DEBUG
- removed net MICROCONTROLLER1:IOREF: MICROCONTROLLER1:U$1.IOREF
- removed net MICROCONTROLLER1:MISO: MICROCONTROLLER1:U$1.MISO_ICSP
- removed net MICROCONTROLLER1:MOSI: MICROCONTROLLER1:U$1.MOSI_ICSP
- removed net MICROCONTROLLER1:NC: MICROCONTROLLER1:U$1.NC
- removed net MICROCONTROLLER1:RESET: MICROCONTROLLER1:U$1.RESET_ICSP
- removed net MICROCONTROLLER1:SCK: MICROCONTROLLER1:U$1.SCK_ICSP
- removed net MICROCONTROLLER1:SCL1: MICROCONTROLLER1:U$1.SCL1
- removed net MICROCONTROLLER1:SDA1: MICROCONTROLLER1:U$1.SDA1
- new net MICROCONTROLLER1:A12: MICROCONTROLLER1:U$1.A12
- new net MICROCONTROLLER1:A13: MICROCONTROLLER1:U$1.A13
- new net MICROCONTROLLER1:A14: MICROCONTROLLER1:U$1.A14
- new net MICROCONTROLLER1:A15: MICROCONTROLLER1:U$1.A15
- net 3V3: now also MICROCONTROLLER1:U$1.3.3V; no longer MICROCONTROLLER1:U$1.3V3
- net GND: now also MICROCONTROLLER1:U$1.GND@0, MICROCONTROLLER1:U$1.GND@1, MICROCONTROLLER1:U$1.GND@2, MICROCONTROLLER1:U$1.GND@3, MICROCONTROLLER1:U$1.GND@4; no longer MICROCONTROLLER1:U$1.5V_ICSP, MICROCONTROLLER1:U$1.GND1, MICROCONTROLLER1:U$1.GND_1, MICROCONTROLLER1:U$1.GND_2, MICROCONTROLLER1:U$1.GND_A, MICROCONTROLLER1:U$1.GND_B
- net MICROCONTROLLER1:5V: now also MICROCONTROLLER1:U$1.5V@0, MICROCONTROLLER1:U$1.5V@1, MICROCONTROLLER1:U$1.5V@2; no longer MICROCONTROLLER1:U$1.5V, MICROCONTROLLER1:U$1.GND_ICSP
- net MICROCONTROLLER1:LED_SCL: now also MICROCONTROLLER1:U$1.21; no longer MICROCONTROLLER1:U$1.SCL
- net MICROCONTROLLER1:LED_SDA: now also MICROCONTROLLER1:U$1.20; no longer MICROCONTROLLER1:U$1.SDA
- net MICROCONTROLLER1:RX0: now also MICROCONTROLLER1:U$1.1; no longer MICROCONTROLLER1:U$1.RX0
- net MICROCONTROLLER1:RX3: now also MICROCONTROLLER1:U$1.15; no longer MICROCONTROLLER1:U$1.RX3
- net MICROCONTROLLER1:TX0: now also MICROCONTROLLER1:U$1.0; no longer MICROCONTROLLER1:U$1.TX0
- net MICROCONTROLLER1:TX2: now also MICROCONTROLLER1:U$1.16; no longer MICROCONTROLLER1:U$1.TX2
- net MICROCONTROLLER1:TX3: now also MICROCONTROLLER1:U$1.14; no longer MICROCONTROLLER1:U$1.TX3
- net N$28: now also MICROCONTROLLER1:U$1.19; no longer MICROCONTROLLER1:U$1.RX1
- net N$29: now also MICROCONTROLLER1:U$1.18; no longer MICROCONTROLLER1:U$1.TX1
- net N$30: now also MICROCONTROLLER1:U$1.17; no longer MICROCONTROLLER1:U$1.RX2
